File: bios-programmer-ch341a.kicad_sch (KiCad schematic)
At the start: 50 parts, among them J1 USB_B_Micro, J2 SPI Debug, J3 I²C Debug, J4 -Banana-, J5 +Banana+, J6 ZIF16, J7 Conn_02x04_Counter_Clockwise, J8 Conn_02x04_Counter_Clockwise, Q1 IRLML6402, Q2 IRLML6402, Q3 IRLML6402, Q4 IRLML6402, SW1 RESET, U1 CH341A, U2 ISO6741, U3 ADuM1252, U4 TL431DBZ, Y1 12M

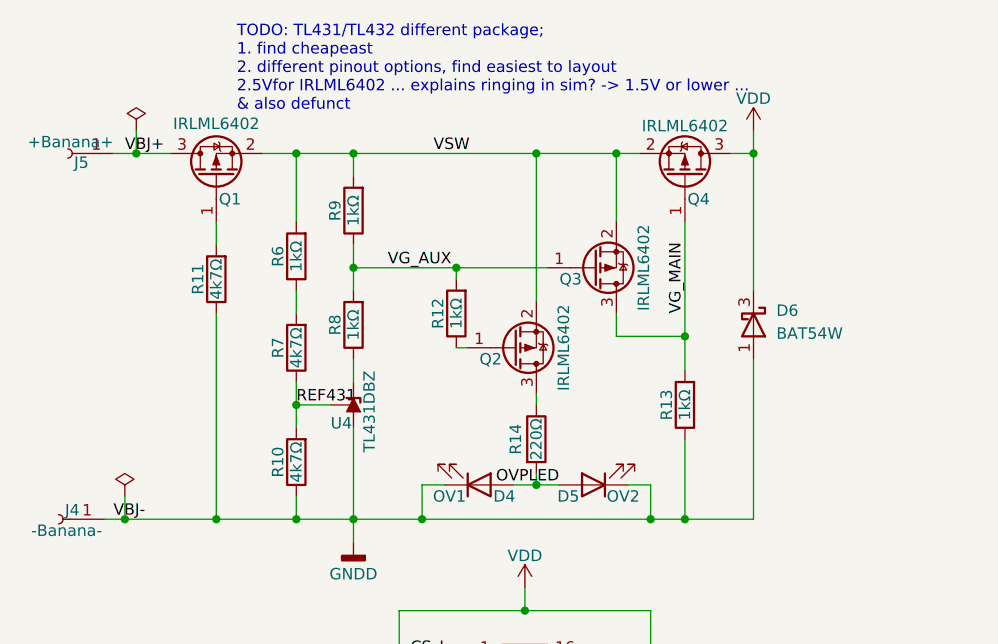
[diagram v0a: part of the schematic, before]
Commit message: PCB: power path protection reasonable layout TODO
probably final version including power-path protection TODO explain some more? first check previous commit, rebase etc

different mosfet! Toshiba thingy
zones for almost everything
wider tracks
and yeah, accidental symbol ...
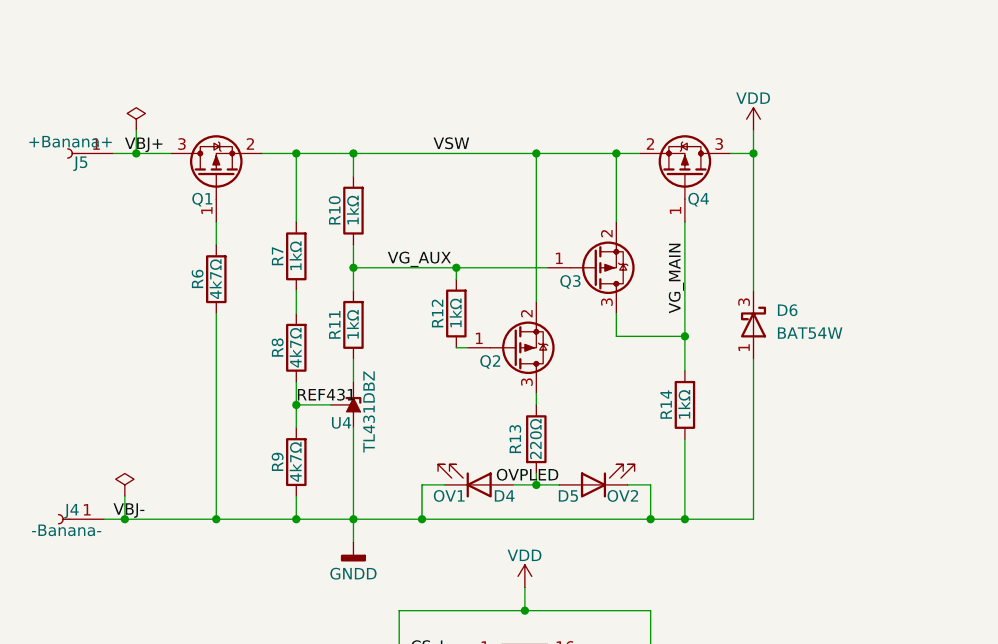
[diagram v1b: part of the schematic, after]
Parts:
- Q1, Q2, Q3, Q4: value IRLML6402 -> SSM3J328R; Mfr (none) -> Toshiba; Part (none) -> SSM3J328R
- renumbered R9 to R10, R8 to R11, R14 to R13, R13 to R14, R11 to R6, R6 to R7, R7 to R8, R10 to R9
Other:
- note removed: "TODO: TL431/TL432 different package; 1. find cheapeast 2. different pinout options, find easiest to layout 2.5Vfor IRLML6402 ... explains ringing in sim? -> 1.5V or lower ... & also defunct"

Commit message: diode removed, zones improved, temp commit?
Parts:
- removed D6: BAT54W, Package_TO_SOT_SMD:SOT-323_SC-70, symbol Diode:BAT54W
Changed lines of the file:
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@@
 	)
 	(junction
-		(at 252.73 62.23)
-		(diameter 0)
-		(color 0 0 0 0)
-	)
-	(junction
 		(at 191.77 21.59)
 		(diameter 0)
@@
 	)
 	(junction
-		(at 260.35 21.59)
-		(diameter 0)
-		(color 0 0 0 0)
-	)
-	(junction
 		(at 220.98 151.13)
 		(diameter 0)
@@
 	(wire
 		(pts
-			(xy 260.35 44.45) (xy 260.35 62.23)
-		)
-		(stroke
-			(width 0)
-			(type default)
-		)
-	)
-	(wire
-		(pts
 			(xy 236.22 21.59) (xy 245.11 21.59)
 		)
@@
 	(wire
 		(pts
-			(xy 260.35 21.59) (xy 260.35 36.83)
-		)
-		(stroke
-			(width 0)
-			(type default)
-		)
-	)
-	(wire
-		(pts
 			(xy 236.22 21.59) (xy 236.22 38.1)
 		)
@@
 	(wire
 		(pts
-			(xy 260.35 62.23) (xy 252.73 62.23)
-		)
-		(stroke
-			(width 0)
-			(type default)
-		)
-	)
-	(wire
-		(pts
 			(xy 166.37 114.3) (xy 166.37 116.84)
 		)
@@
 					(unit 1)
 				)
-			)
-		)
-	)
-	(symbol
-		(lib_id "Diode:BAT54W")
-		(at 260.35 40.64 270)
-		(unit 1)
-		(body_style 1)
-		(exclude_from_sim no)
-		(in_bom yes)
-		(on_board yes)
-		(in_pos_files yes)
-		(dnp no)
-		(fields_autoplaced yes)
-		(property "Reference" "D6"
-			(at 262.89 39.0524 90)
-			(show_name no)
-			(do_not_autoplace no)
-			(effects
-				(font
-					(size 1.27 1.27)
-				)
-				(justify left)
-			)
-		)
-		(property "Value" "BAT54W"
-			(at 262.89 41.5924 90)
-			(show_name no)
-			(do_not_autoplace no)
-			(effects
-				(font
-					(size 1.27 1.27)
-				)
-				(justify left)
-			)
-		)
-		(property "Footprint" "Package_TO_SOT_SMD:SOT-323_SC-70"
-			(at 255.905 40.64 0)
-			(hide yes)
-			(show_name no)
-			(do_not_autoplace no)
-			(effects
-				(font
-					(size 1.27 1.27)
-				)
-			)
-		)
-		(property "Datasheet" "https://assets.nexperia.com/documents/data-sheet/BAT54W_SER.pdf"
-			(at 260.35 40.64 0)
-			(hide yes)
-			(show_name no)
-			(do_not_autoplace no)
-			(effects
-				(font
-					(size 1.27 1.27)
-				)
-			)
-		)
-		(property "Description" "Schottky barrier diode, SOT-323"
-			(at 260.35 40.64 0)
-			(hide yes)
-			(show_name no)
-			(do_not_autoplace no)
-			(effects
-				(font
-					(size 1.27 1.27)
-				)
-			)
-		)
-		(pin "1"
-		)
-		(pin "2"
-		)
-		(pin "3"
-		)
-		(instances
-			(project "bios-programmer-ch341a"
-				(path "/a99a5965-7ad8-4ba1-a50b-0a8ec2909645"
-					(reference "D6")
-					(unit 1)
-				)

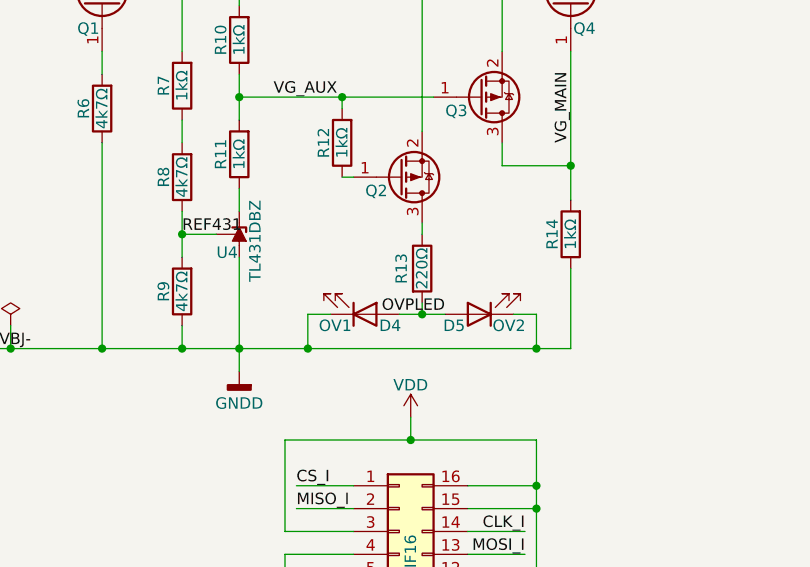
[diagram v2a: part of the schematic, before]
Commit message: PCB: moved OVP LED tracks down, added LED resistor and some beautification
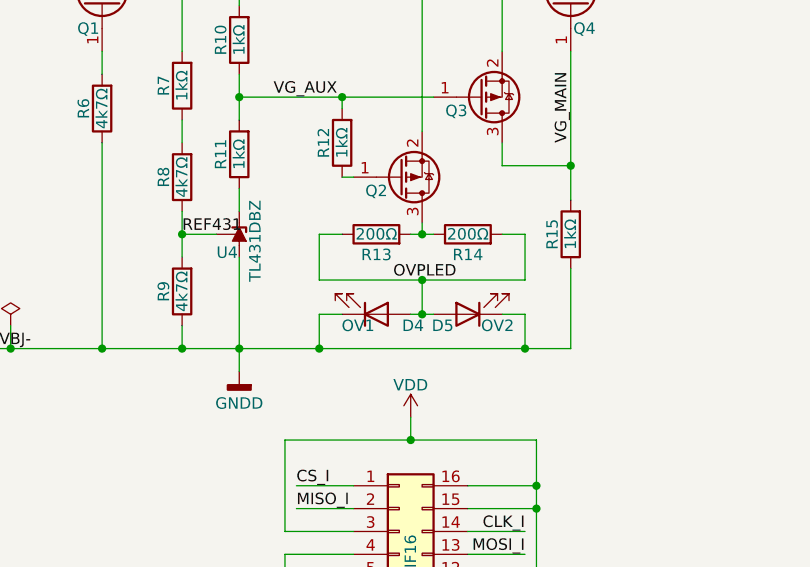
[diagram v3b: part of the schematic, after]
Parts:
- added R14: 200Ω, Resistor_SMD:R_0603_1608Metric_Pad0.98x0.95mm_HandSolder, symbol Device:R
- R13: value 220Ω -> 200Ω
- renumbered R14 to R15
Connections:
- net OVPLED: now also R13.1, R14.2; no longer R13.2
- net at Q2.3 (D): now also R13.2, R14.1; no longer R13.1
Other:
- moved on the sheet: D4, D5, R13

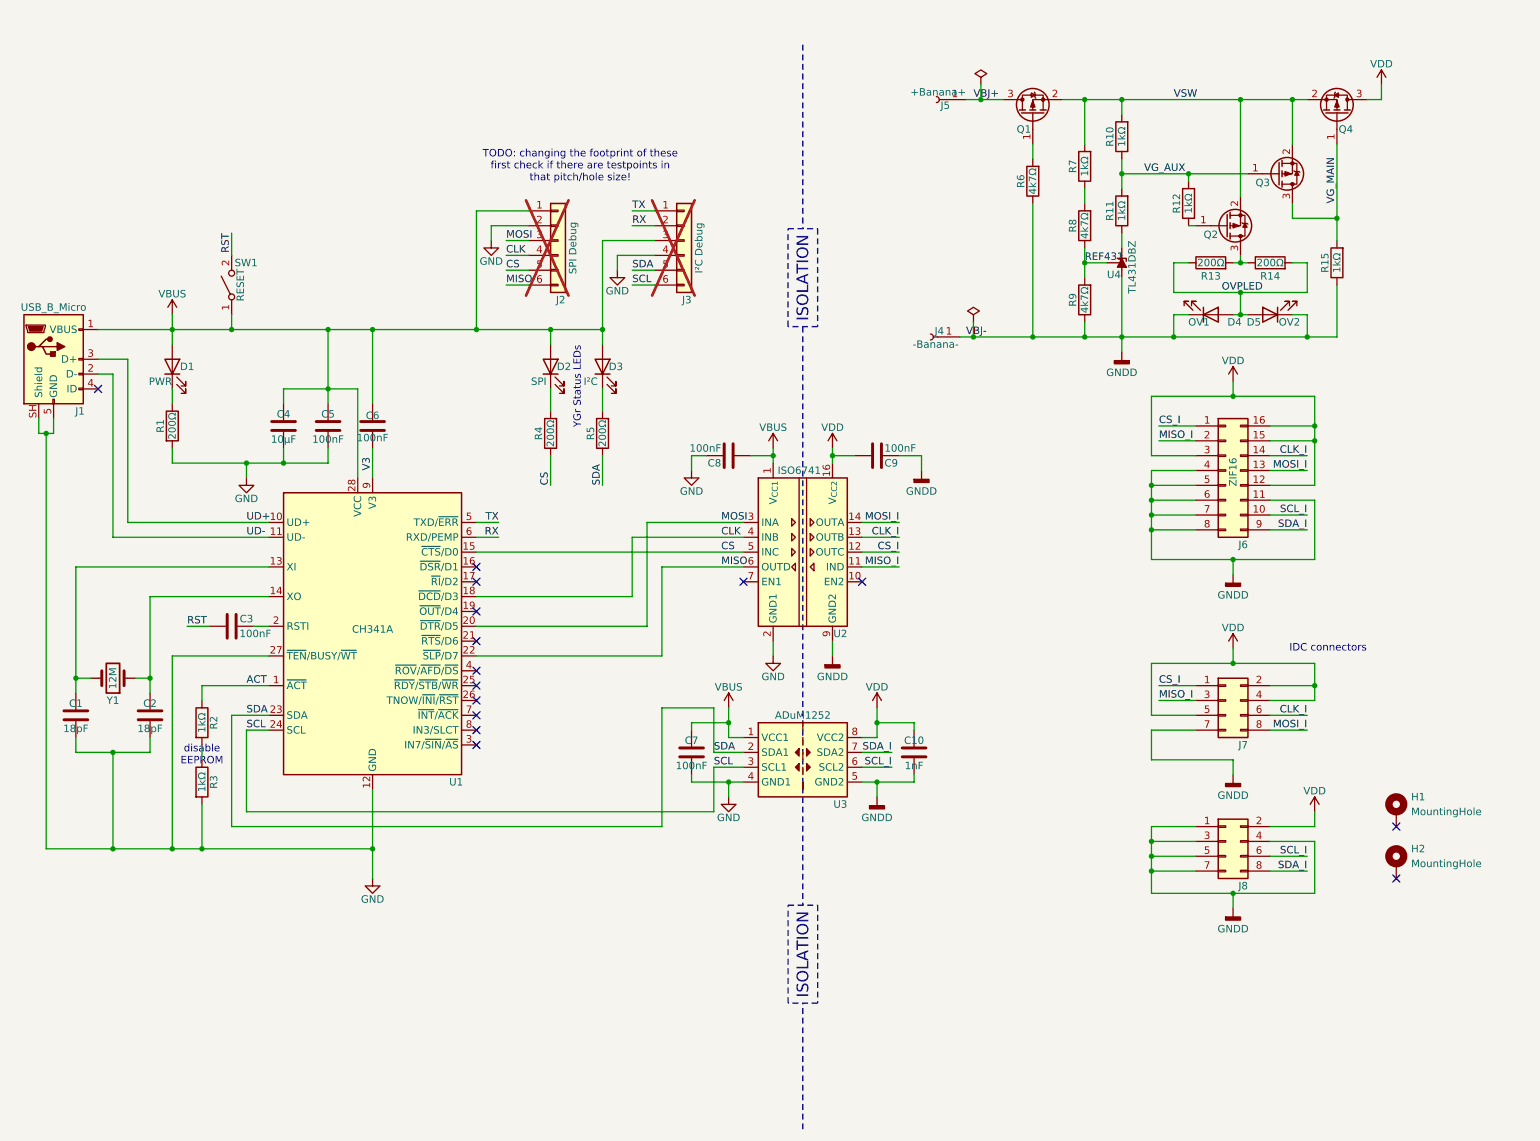
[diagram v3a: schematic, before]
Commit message: SCH/PCB: 1% 5.6K resistor instead of 4.7K (1%) + 1K (5%)
Technically this would have worked as-is, since the 5% for the 1K results in
only a small change to the total resistance. The resulting voltage would be
(according to SPICE) between 5.3V and 5.49V, compared to 5.3V and 5.41V.

On the other hand I would expect a 1% resistor to also have a better tolerance
to temperature changes, which I did not simulate with actual resistor models.

The TL432 requires precise resistors if I want this OVP to work reliably.
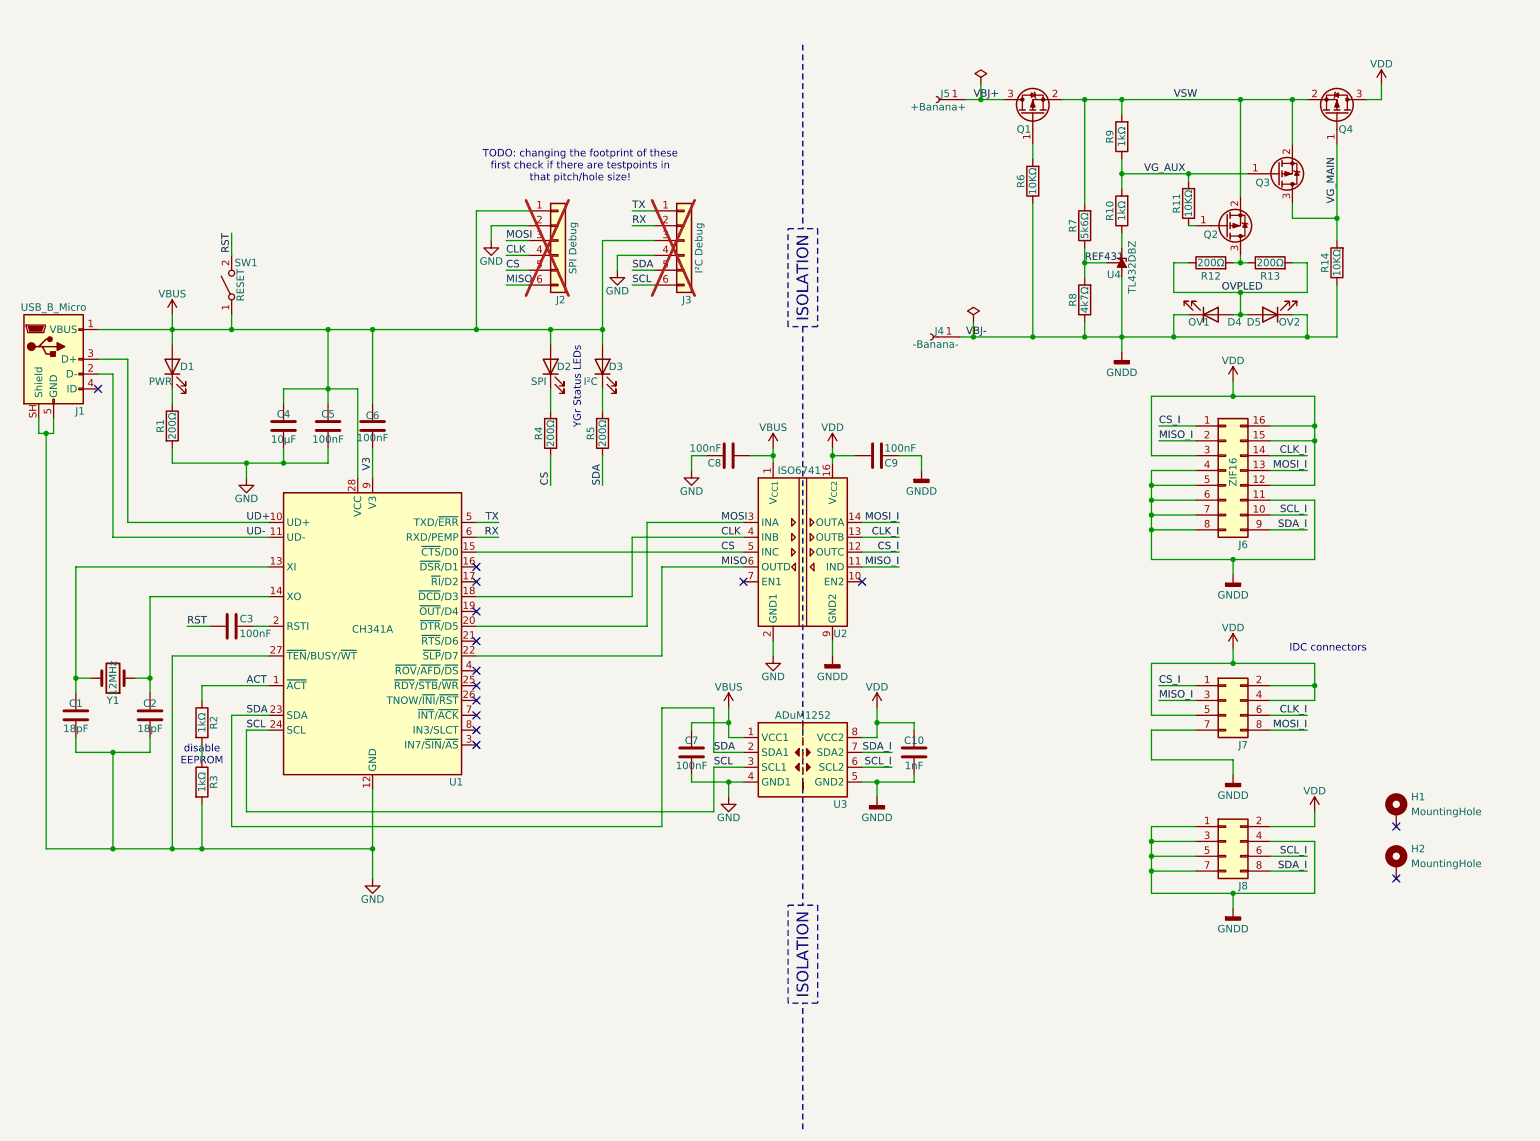
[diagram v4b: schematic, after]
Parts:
- removed R7: 1kΩ, Resistor_SMD:R_0603_1608Metric_Pad0.98x0.95mm_HandSolder, symbol Device:R
- R11: renamed from R12; value 1kΩ -> 10KΩ
- R14: renamed from R15; value 1kΩ -> 10KΩ
- R6: value 4k7Ω -> 10KΩ
- R7: renamed from R8; value 4k7Ω -> 5k6Ω
- U1: Mfr (none) -> WCH; Part (none) -> CH341(A|B)
- U2: Mfr (none) -> Texas Instruments
- U4: value TL431DBZ -> TL432DBZ; Mfr (none) -> Texas Instruments; Part (none) -> TL432DBZ
- Y1: value 12M -> 12MHz
- renumbered R11 to R10, R13 to R12, R14 to R13, R9 to R8, R10 to R9
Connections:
- net VSW: now also R7.2
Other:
- moved on the sheet: J5

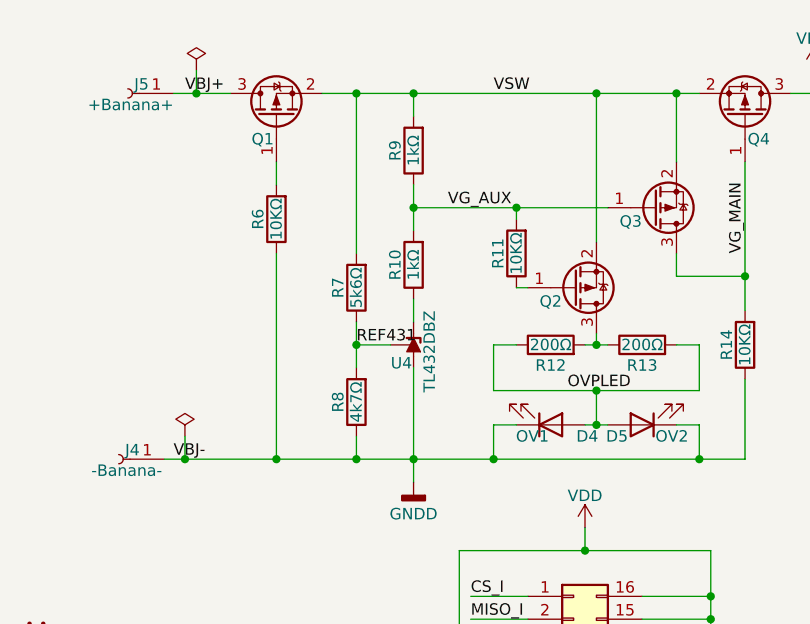
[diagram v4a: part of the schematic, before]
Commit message: PCB increase clearances, no need to be tight; increased track widths; nets for all non-default?
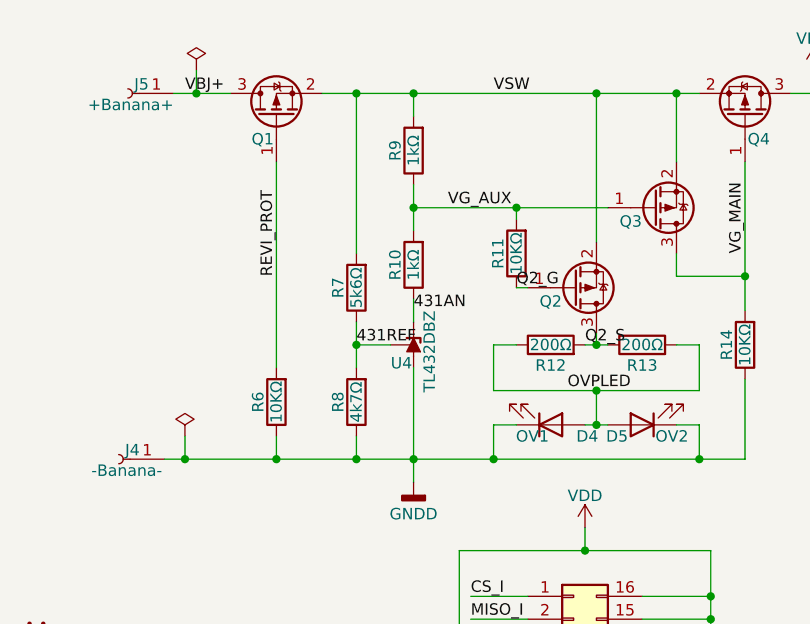
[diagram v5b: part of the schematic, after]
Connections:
- net REVI_PROT: now reaches Q1.1 (G), R6.2
- net Q2_G: now reaches Q2.1 (G), R11.1
- net Q2_S: now reaches Q2.3 (D), R12.2, R13.1
- net 431AN: now reaches R10.1, U4.2 (K)
- net REF431 renamed 431REF
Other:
- moved on the sheet: R6
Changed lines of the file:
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@@
 	(wire
 		(pts
-			(xy 200.66 39.37) (xy 200.66 62.23)
-		)
-		(stroke
-			(width 0)
-			(type default)
-		)
-	)
-	(wire
-		(pts
 			(xy 53.34 58.42) (xy 53.34 60.96)
 		)
@@
 	(wire
 		(pts
-			(xy 200.66 29.21) (xy 200.66 31.75)
+			(xy 200.66 29.21) (xy 200.66 52.07)
 		)
 		(stroke
@@
 	(wire
 		(pts
+			(xy 200.66 59.69) (xy 200.66 62.23)
+		)
+		(stroke
+			(width 0)
+			(type default)
+		)
+	)
+	(wire
+		(pts
 			(xy 171.45 93.98) (xy 177.8 93.98)
 		)
@@
 		)
 	)
+	(label "REVI_PROT"
+		(at 200.66 41.91 90)
+		(effects
+			(font
+				(size 1.27 1.27)
+			)
+			(justify left bottom)
+		)
+	)
 	(label "RST"
 		(at 55.88 111.76 0)
@@
 		)
 	)
-	(label "REF431"
+	(label "431REF"
 		(at 209.55 49.53 0)
 		(effects
@@
 		)
 	)
+	(label "Q2_S"
+		(at 234.95 49.53 0)
+		(effects
+			(font
+				(size 1.27 1.27)
+			)
+			(justify left bottom)
+		)
+	)
 	(label "SCL_I"
 		(at 247.65 92.71 180)
@@
 		)
 	)
+	(label "Q2_G"
+		(at 227.33 43.18 0)
+		(effects
+			(font
+				(size 1.27 1.27)
+			)
+			(justify left bottom)
+		)
+	)
 	(label "SDA_I"
 		(at 247.65 95.25 180)
@@
 		)
 	)
-	(label "VBJ-"
-		(at 189.23 62.23 0)
-		(effects
-			(font
-				(size 1.27 1.27)
-			)
-			(justify left bottom)
-		)
-	)
 	(label "CLK_I"
 		(at 247.65 127 180)
@@
 		)
 	)
+	(label "431AN"
+		(at 215.9 45.72 0)
+		(effects
+			(font
+				(size 1.27 1.27)
+			)
+			(justify left bottom)
+		)
+	)
 	(symbol
 		(lib_id "Connector_Generic:Conn_01x06")
@@
 	(symbol
 		(lib_id "Device:R")
-		(at 200.66 35.56 180)
+		(at 200.66 55.88 180)
 		(unit 1)
 		(body_style 1)
@@
 		(dnp no)
 		(property "Reference" "R6"
-			(at 198.628 35.56 90)
+			(at 198.628 55.88 90)
 			(show_name no)
 			(do_not_autoplace no)
@@
 		)
 		(property "Value" "10KΩ"
-			(at 200.66 35.56 90)
+			(at 200.66 55.88 90)
 			(show_name no)
 			(do_not_autoplace no)
@@
 		)
 		(property "Footprint" "Resistor_SMD:R_0603_1608Metric_Pad0.98x0.95mm_HandSolder"
-			(at 202.438 35.56 90)
+			(at 202.438 55.88 90)
 			(hide yes)
 			(show_name no)
@@
 		)
 		(property "Datasheet" ""
-			(at 200.66 35.56 0)
+			(at 200.66 55.88 0)
 			(hide yes)
 			(show_name no)
@@
 		)
 		(property "Description" "10KΩ, 0603, 5%"
-			(at 200.66 35.56 0)
+			(at 200.66 55.88 0)
 			(hide yes)
 			(show_name no)

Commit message: adding sense wires; beautification; issue with 2x05 IDC connector on top of isolator to be fixed
PCB temp bijna sense zonde bovenkant

pcb sense on bottom done; cleanup todo
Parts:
- added J9: SENSE, TerminalBlock_TE-Connectivity:TerminalBlock_TE_282834-2_1x02_P2.54mm_Horizontal, symbol Connector:Screw_Terminal_01x02
- J7, J8: value Conn_02x04_Counter_Clockwise -> Conn_02x05_Odd_Even; footprint Connector_IDC:IDC-Header_2x04_P2.54mm_Horizontal -> footprints:IDC-Header_2x05_P2.54mm_Horizontal_1.64mm_pad; symbol Connector_Generic:Conn_02x04_Odd_Even -> Connector_Generic:Conn_02x05_Odd_Even
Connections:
- net CLK_I: now also J7.8 (Pin_8); no longer J7.6 (Pin_6)
- net CS_I: now also J7.3 (Pin_3); no longer J7.1 (Pin_1)
- net GNDD: now also J7.9 (Pin_9), J8.6 (Pin_6), J8.9 (Pin_9); no longer J7.7 (Pin_7), J8.1 (Pin_1), J8.4 (Pin_4)
- net MISO_I: now also J7.5 (Pin_5); no longer J7.3 (Pin_3)
- net MOSI_I: now also J7.10 (Pin_10); no longer J7.8 (Pin_8)
- net SCL_I: now also J8.8 (Pin_8); no longer J8.6 (Pin_6)
- net SDA_I: now also J8.10 (Pin_10); no longer J8.8 (Pin_8)
- net VDD: now also J7.6 (Pin_6), J7.7 (Pin_7), J8.4 (Pin_4); no longer J7.2 (Pin_2), J7.5 (Pin_5), J8.2 (Pin_2)
- new net SNS+: J7.2 (Pin_2), J8.2 (Pin_2), J9.1 (Pin_1)
- new net SNS-: J7.1 (Pin_1), J8.1 (Pin_1), J9.2 (Pin_2)
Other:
- note removed: "IDC connectors"
- moved on the sheet: H1, H2, J6
